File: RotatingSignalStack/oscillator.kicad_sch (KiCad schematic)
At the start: 3 parts, among them J1 Conn_01x02, U3 SN65HVD232

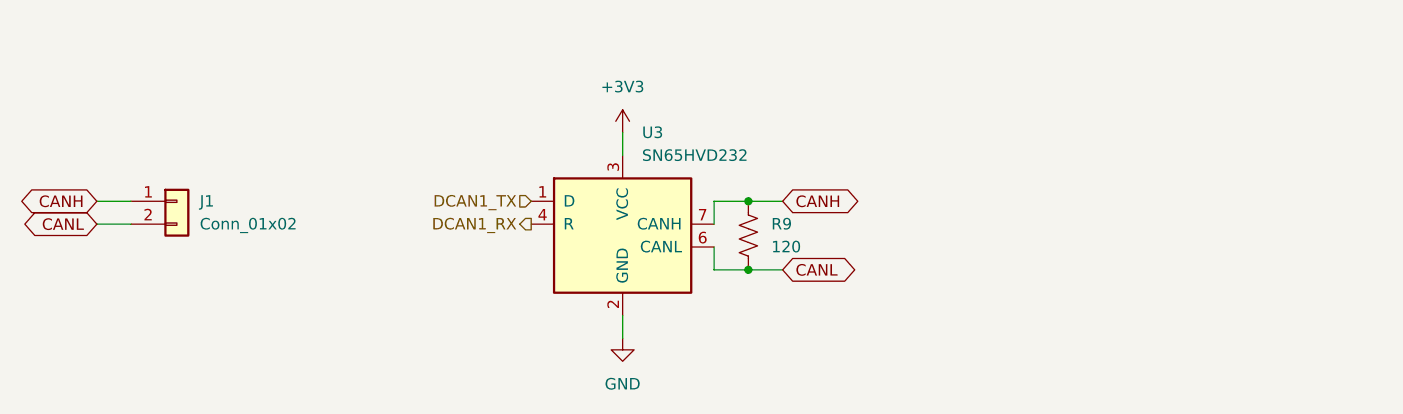
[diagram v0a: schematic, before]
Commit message: Added Oscillator, New Magnetics, Sheet Pins
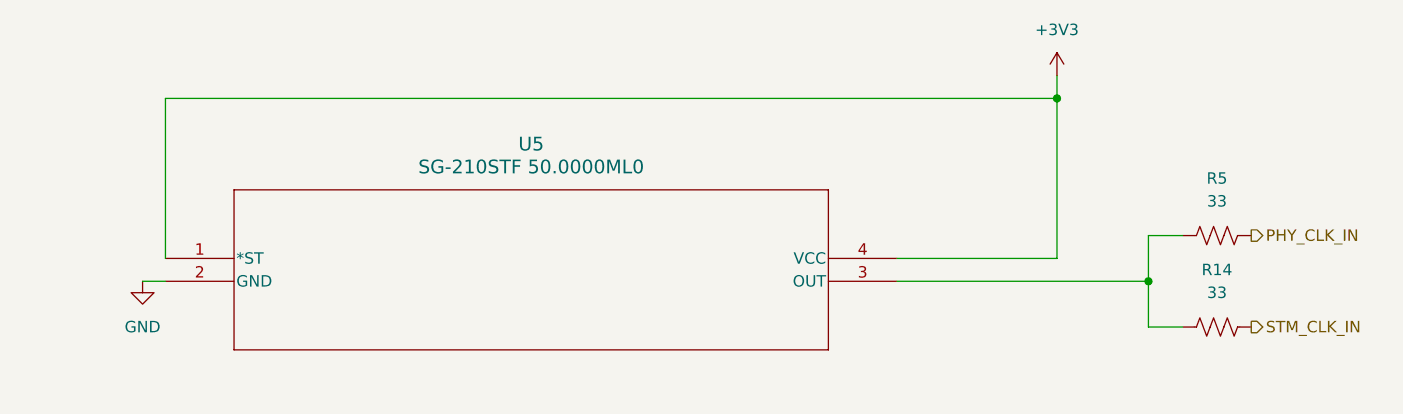
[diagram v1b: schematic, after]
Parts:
- removed J1: Conn_01x02, Connector_JST:JST_SH_SM02B-SRSS-TB_1x02-1MP_P1.00mm_Horizontal, symbol Connector_Generic:Conn_01x02
- removed R9: 120, symbol Device:R_US
- removed U3: SN65HVD232, Package_SO:SOIC-8_3.9x4.9mm_P1.27mm, symbol Interface_CAN_LIN:SN65HVD232
- added R14, R5: 33, symbol Device:R_US
- added U5: SG-210STF 50.0000ML0, SG-210STF 50.0000ML0_EPS, symbol SG-210STF 50.0000ML0:SG-210STF_50.0000ML0
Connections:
- net +3V3: now also U5.1 (*ST), U5.4 (VCC)
- net GND: now also U5.2 (GND)
- new net: R14.1, R5.1, U5.3 (OUT)
- new net PHY_CLK_IN: R5.2
- new net STM_CLK_IN: R14.2

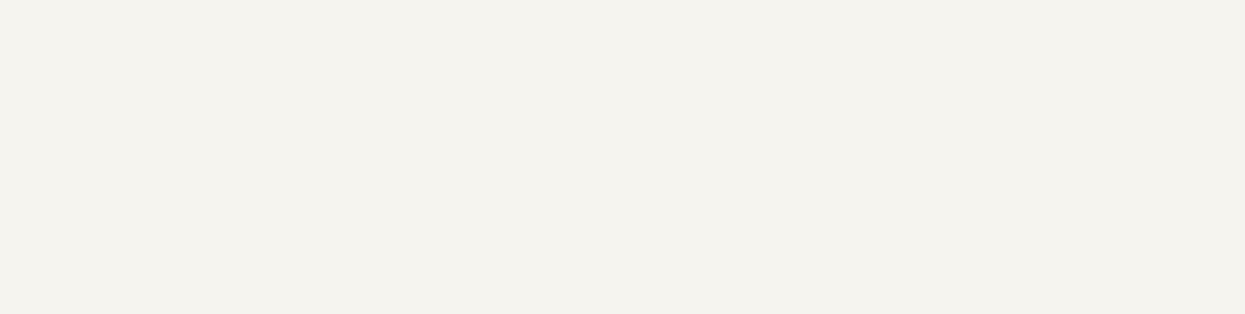
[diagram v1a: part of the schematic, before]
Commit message: STM design and ESD protection
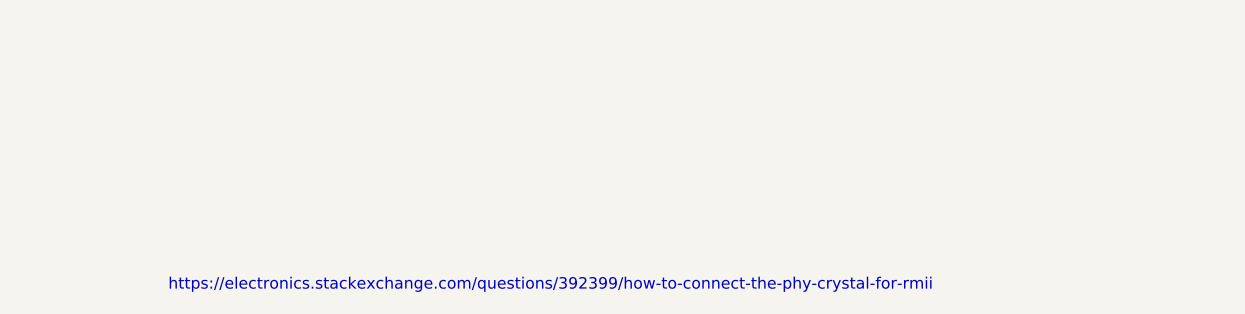
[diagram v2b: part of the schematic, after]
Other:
- note added: "https://electronics.stackexchange.com/questions/392399/how-to-connect-the-phy-crystal-for-rmii"
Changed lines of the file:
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@@
 	(generator_version "9.0")
 	(paper "A4")
+	(text "https://electronics.stackexchange.com/questions/392399/how-to-connect-the-phy-crystal-for-rmii"
+		(exclude_from_sim no)
+		(at 75.438 151.638 0)
+		(effects
+			(font
+				(size 1.27 1.27)
+			)
+		)
+	)
 	(junction
 		(at 205.74 82.55)
